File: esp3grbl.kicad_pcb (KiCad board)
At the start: 2 copper layers, 7 parts, among them J1 Conn_02x19_Odd_Even, J2 Conn_02x19_Odd_Even, J3 Z axis, J4 Y1-Axis, J5 Y2 - Axis, J6 x - axis, U1 ESP32-DEVKITC-32D

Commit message: v0
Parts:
- added C1: 0.33uF, Capacitor_THT:CP_Axial_L11.0mm_D5.0mm_P18.00mm_Horizontal, F.Cu at (111.8, 47.0)
- added C2: 1uF, Capacitor_THT:CP_Axial_L11.0mm_D5.0mm_P18.00mm_Horizontal, F.Cu at (148.6, 53.3)
- added C3: 0.1uF, Capacitor_THT:C_Disc_D6.0mm_W4.4mm_P5.00mm, F.Cu at (154.9, 44.5)
- added C4: 0.1uF, Capacitor_THT:C_Disc_D6.0mm_W4.4mm_P5.00mm, F.Cu at (174.0, 113.0)
- added C5: 0.1uF, Capacitor_THT:C_Disc_D6.0mm_W4.4mm_P5.00mm, F.Cu at (177.8, 100.3)
- added C6: 0.1uF, Capacitor_THT:C_Disc_D6.0mm_W4.4mm_P5.00mm, F.Cu at (184.2, 116.8)
- added C7: 0.1uF, Capacitor_THT:C_Disc_D6.0mm_W4.4mm_P5.00mm, F.Cu at (176.5, 86.4)
- added D2: D_Schottky, Diode_THT:D_A-405_P12.70mm_Horizontal, F.Cu at (148.6, 66.0)
- added D3: D, Diode_THT:D_A-405_P10.16mm_Horizontal, F.Cu at (186.7, 71.1)
- added D4: D, Diode_THT:D_A-405_P10.16mm_Horizontal, F.Cu at (186.7, 63.5)
- added D5: D, Diode_THT:D_A-405_P10.16mm_Horizontal, F.Cu at (186.7, 58.4)
- added D6: D, Diode_THT:D_A-405_P10.16mm_Horizontal, F.Cu at (170.2, 116.8)
- added J10: x - axis, Connector_Phoenix_MSTB:PhoenixContact_MSTBA_2,5_6-G-5,08_1x06_P5.08mm_Horizontal, F.Cu at (175.3, 128.3)
- added J11: Outputs, Connector_Phoenix_MSTB:PhoenixContact_MSTBA_2,5_4-G-5,08_1x04_P5.08mm_Horizontal, F.Cu at (193.0, 68.6)
- added J12: Micro_SD_Card_Adater, Connector_PinHeader_2.54mm:PinHeader_1x06_P2.54mm_Vertical, F.Cu at (90.2, 47.0)
- added J13: Probe, Connector_Phoenix_MSTB:PhoenixContact_MSTBA_2,5_2-G-5,08_1x02_P5.08mm_Horizontal, F.Cu at (193.0, 109.2)
- added J14: Buttons, Connector_Phoenix_MSTB:PhoenixContact_MSTBA_2,5_4-G-5,08_1x04_P5.08mm_Horizontal, F.Cu at (193.0, 94.0)
- added J7: Z axis, Connector_Phoenix_MSTB:PhoenixContact_MSTBA_2,5_6-G-5,08_1x06_P5.08mm_Horizontal, F.Cu at (68.6, 128.3)
- added J8: Y1-Axis, Connector_Phoenix_MSTB:PhoenixContact_MSTBA_2,5_6-G-5,08_1x06_P5.08mm_Horizontal, F.Cu at (104.1, 128.3)
- added J9: Y2 - Axis, Connector_Phoenix_MSTB:PhoenixContact_MSTBA_2,5_6-G-5,08_1x06_P5.08mm_Horizontal, F.Cu at (139.7, 128.3)
- added R1: 1k, Resistor_THT:R_Axial_DIN0207_L6.3mm_D2.5mm_P7.62mm_Horizontal, F.Cu at (74.9, 57.1)
- added R10: 10k, Resistor_THT:R_Axial_DIN0207_L6.3mm_D2.5mm_P7.62mm_Horizontal, F.Cu at (148.6, 110.5)
- added R11: 10k, Resistor_THT:R_Axial_DIN0207_L6.3mm_D2.5mm_P7.62mm_Horizontal, F.Cu at (148.6, 99.1)
- added R12: 10k, Resistor_THT:R_Axial_DIN0207_L6.3mm_D2.5mm_P7.62mm_Horizontal, F.Cu at (171.4, 104.1)
- added R13: 10k, Resistor_THT:R_Axial_DIN0207_L6.3mm_D2.5mm_P7.62mm_Horizontal, F.Cu at (148.6, 86.4)
- added R2: 1k, Resistor_THT:R_Axial_DIN0207_L6.3mm_D2.5mm_P7.62mm_Horizontal, F.Cu at (74.9, 81.3)
- added R3: 1k, Resistor_THT:R_Axial_DIN0207_L6.3mm_D2.5mm_P7.62mm_Horizontal, F.Cu at (63.5, 121.9)
- added R4: 1k, Resistor_THT:R_Axial_DIN0207_L6.3mm_D2.5mm_P7.62mm_Horizontal, F.Cu at (74.9, 105.4)
- added R5: R163, Resistor_THT:R_Axial_DIN0207_L6.3mm_D2.5mm_P7.62mm_Horizontal, F.Cu at (156.2, 59.7)
- added R6: 10k, Resistor_THT:R_Axial_DIN0207_L6.3mm_D2.5mm_P7.62mm_Horizontal, F.Cu at (83.8, 54.6)
- added R7: 10k, Resistor_THT:R_Axial_DIN0207_L6.3mm_D2.5mm_P7.62mm_Horizontal, F.Cu at (83.8, 78.7)
- added R8: 10k, Resistor_THT:R_Axial_DIN0207_L6.3mm_D2.5mm_P7.62mm_Horizontal, F.Cu at (83.8, 102.9)
- added R9: 10k, Resistor_THT:R_Axial_DIN0207_L6.3mm_D2.5mm_P7.62mm_Horizontal, F.Cu at (83.8, 116.8)
- added SW1: Canel, Button_Switch_THT:SW_PUSH_6mm, F.Cu at (163.8, 108.0)
- added SW2: Play, Button_Switch_THT:SW_PUSH_6mm, F.Cu at (163.8, 95.2)
- added SW3: SW_Push, Button_Switch_THT:SW_PUSH_6mm, F.Cu at (163.8, 82.5)
- added U2: PC817, Package_DIP:DIP-4_W7.62mm, F.Cu at (67.3, 71.1)
- added U3: PC817, Package_DIP:DIP-4_W7.62mm, F.Cu at (67.3, 95.2)
- added U4: PC817, Package_DIP:DIP-4_W7.62mm, F.Cu at (67.3, 114.3)
- added U5: L7805, Package_TO_SOT_THT:TO-220F-3_Vertical, F.Cu at (135.9, 47.0)
- added U6: ESP32-DEVKITC-32D, lib:MODULE_ESP32-DEVKITC-32D, F.Cu at (124.5, 85.1)
- J1: value Conn_02x19_Odd_Even -> Emergency Stop; footprint Connector_PinSocket_2.54mm:PinSocket_2x19_P2.54mm_Vertical -> Connector_Phoenix_MC_HighVoltage:PhoenixContact_MCV_1,5_2-G-5.08_1x02_P5.08mm_Vertical
- J2: value Conn_02x19_Odd_Even -> Power Supply; footprint Connector_PinSocket_2.54mm:PinSocket_2x19_P2.54mm_Vertical -> Connector_Phoenix_MC_HighVoltage:PhoenixContact_MCV_1,5_2-G-5.08_1x02_P5.08mm_Vertical
- J3: value Z axis -> Y1 Limit
- J4: value Y1-Axis -> X Limit
- J5: value Y2 - Axis -> Y2 Limit
- J6: value x - axis -> Z limit
- U1: value ESP32-DEVKITC-32D -> PC817; footprint ESP32 DevKit C:MODULE_ESP32-DEVKITC-32D -> Package_DIP:DIP-4_W7.62mm
- moved J1 199.1 mm to (184.2, 44.5), turned to 180 degrees
- moved U1 80.0 mm to (67.3, 47.0)
- moved J2 33.5 mm to (165.1, 44.5), turned to 180 degrees
- moved J6 18.9 mm to (57.1, 119.4)
- moved J5 17.3 mm to (57.1, 95.2)
- moved J4 15.9 mm to (57.1, 71.1)
- moved J3 15.3 mm to (57.1, 47.0)
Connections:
- J1 pad 1: Net-(J1-Pad1) -> /12VDC
- J1 pad 2: Net-(J1-Pad2) -> /12V
- J2 pad 1: Net-(J2-Pad1) -> /12V
- J2 pad 2: Net-(J2-Pad2) -> GND
- J3 pad 1: /z-dir -> +12V
- J3 pad 2: /z-step -> (no net)
- J3 pad 3: /x-enable -> Net-(J3-Pad3)
- J3 pad 4: Net-(J3-Pad4) -> GND
- J4 pad 1: /y1-dir -> +12V
- J4 pad 2: /y1-step -> (no net)
- J4 pad 3: /x-enable -> Net-(J4-Pad3)
- J4 pad 4: Net-(J4-Pad4) -> GND
- J5 pad 1: /y2-dir -> +12V
- J5 pad 2: /y2-step -> (no net)
- J5 pad 3: /x-enable -> Net-(J5-Pad3)
- J5 pad 4: Net-(J5-Pad4) -> GND
- J6 pad 1: /x-dir -> +12V
- J6 pad 2: /x-step -> (no net)
- J6 pad 3: /x-enable -> Net-(J6-Pad3)
- J6 pad 4: Net-(J6-Pad4) -> GND
- U1 pad 1: Net-(U1-Pad1) -> +12V
- U1 pad 3: Net-(U1-Pad3) -> GND
- U1 pad 4: Net-(U1-Pad4) -> /GPIO_NUM_36
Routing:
- net GND: track 0.00 -> 854.2 mm, vias 0 -> 4
- net +12V: track 0.00 -> 455.6 mm
- net +5V: track 0.00 -> 403.4 mm, vias 0 -> 1
- net +3V3: track 0.00 -> 284.0 mm
- net /x-enable: track 89.9 -> 207.3 mm
- net Cancel: track 0.00 -> 114.6 mm
- net /x-step: track 110.0 -> 0.00 mm
- net /x-dir: track 103.6 -> 0.00 mm
- net /GPIO_NUM_13: track 0.00 -> 98.1 mm
- net /z-step: track 95.6 -> 0.00 mm
- net /GPIO_NUM_12: track 0.00 -> 91.0 mm
- net /SCK: track 0.00 -> 87.8 mm
- net Pause: track 0.00 -> 87.5 mm
- net /CS: track 0.00 -> 84.0 mm
- net /GPIO_NUM_14: track 0.00 -> 80.9 mm
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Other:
- net class +12V added: clearance 0.5, trace_width 2, via_dia 0.8, via_drill 0.4
- net class Default: clearance 0.2 -> 0.5; trace_width 0.25 -> 1
- net class GND added: clearance 0.5, trace_width 1, via_dia 2, via_drill 0.6
- rule trace_clearance: 0.2 -> 0.5

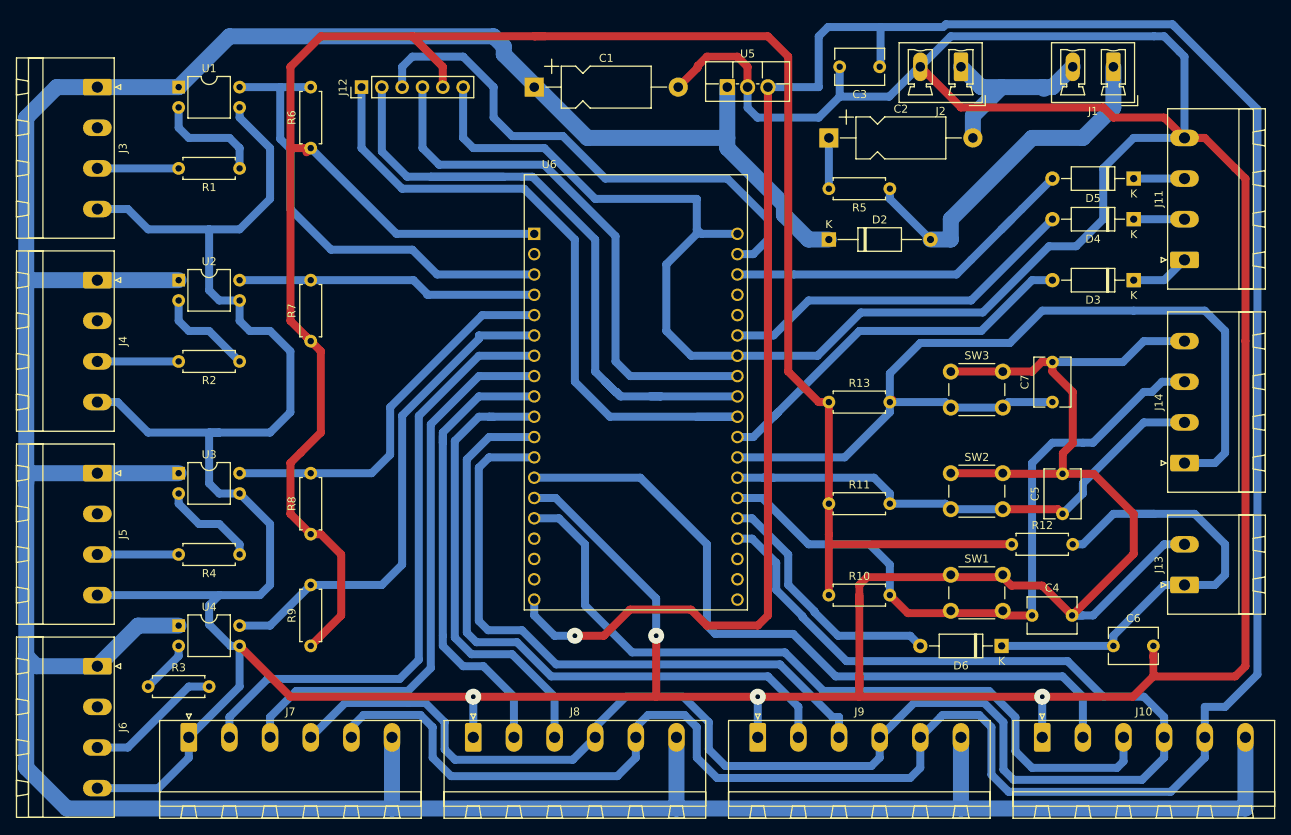
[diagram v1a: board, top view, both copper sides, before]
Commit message: Refine layout and screen mask
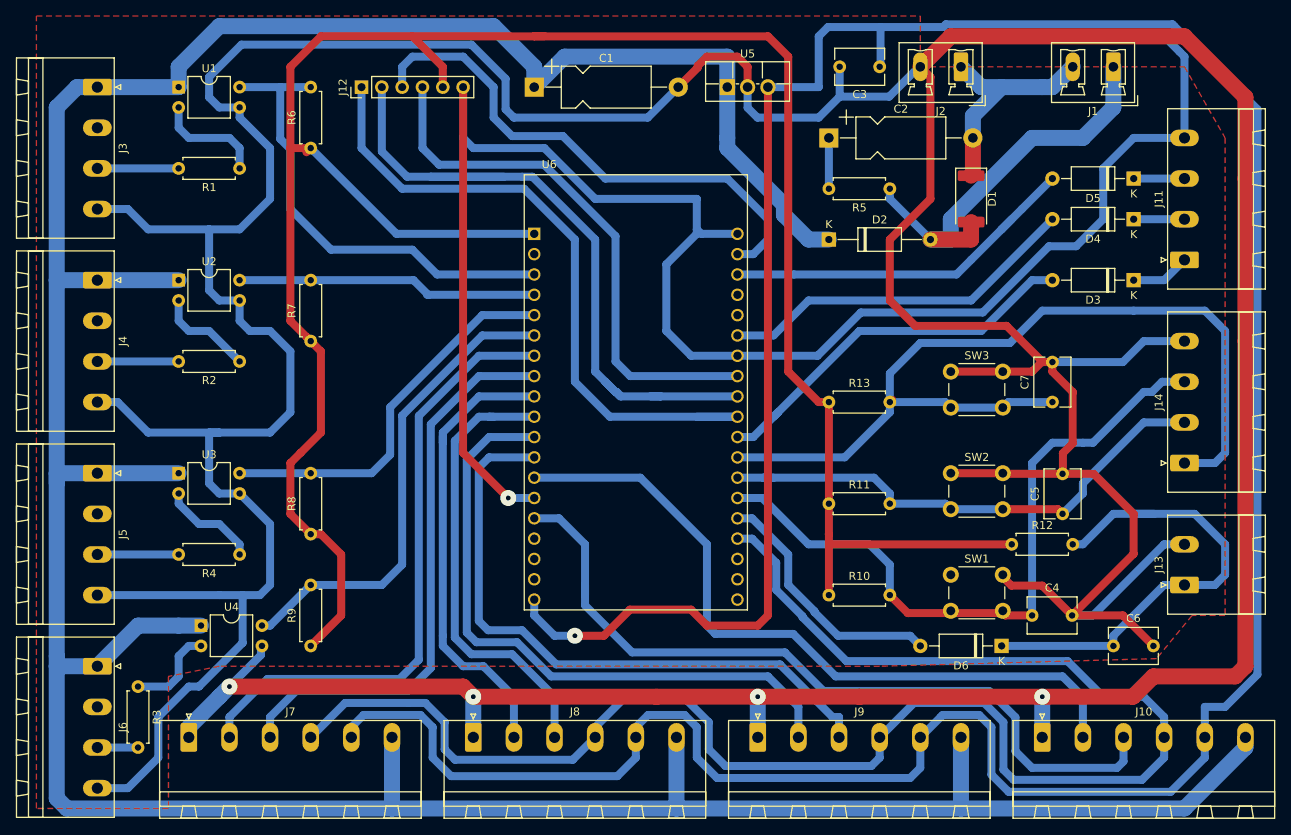
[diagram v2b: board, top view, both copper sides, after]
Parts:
- added D1: D_TVS, Diode_SMD:D_2512_6332Metric, F.Cu at (166.4, 61.0)
- moved U4 2.79 mm to (70.1, 114.3)
- moved R3 1.27 mm to (62.2, 121.9), turned to 270 degrees
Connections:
- J3 pad 2: (no net) -> Net-(J3-Pad2)
- J4 pad 2: (no net) -> Net-(J4-Pad2)
- J5 pad 2: (no net) -> Net-(J5-Pad2)
- J6 pad 2: (no net) -> Net-(J6-Pad2)
- U6 pad 16: (no net) -> Net-(U6-Pad16)
- U6 pad 17: (no net) -> Net-(U6-Pad17)
- U6 pad 18: (no net) -> Net-(U6-Pad18)
- U6 pad 2: (no net) -> Net-(U6-Pad2)
- U6 pad 23: (no net) -> Net-(U6-Pad23)
- U6 pad 24: (no net) -> Net-(U6-Pad24)
- U6 pad 36: (no net) -> Net-(U6-Pad36)
- U6 pad 37: (no net) -> Net-(U6-Pad37)
- U6 pad 38: (no net) -> Net-(U6-Pad38)
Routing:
- net GND: track 854.2 -> 999.8 mm, vias 4 -> 5
- net Net-(J6-Pad3): track 17.1 -> 5.08 mm
- net +12V: track 455.6 -> 444.1 mm
- net /12VDC: track 44.7 -> 52.0 mm
- net Net-(R3-Pad1): track 6.66 -> 11.5 mm
- net /12V: track 24.2 -> 28.7 mm
- net /GPIO_NUM_35: track 62.8 -> 60.0 mm
- added copper zone on F.Cu, net GND
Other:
- board text added: "+12V"
- board text added: "+5V"
- board text added: "12V"
- board text added: "AUX"
- board text added: "CANCEL"
- board text added: "COOLANT"
- board text added: "CS"
- board text added: "DIR"
- board text added: "ENABLE"
- board text added: "GND"
- board text added: "PAUSE"
- board text added: "PLAY"
- board text added: "PROBE"
- board text added: "SPIN_PWM"
- board text added: "STEP"
- board text added: "X1"
- board text added: "Y1"
- board text added: "Y2"
- board text added: "Z1"
